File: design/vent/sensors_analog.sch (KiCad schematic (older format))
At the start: 7 parts, among them J1 A-DF 15 A/KG-T2S, U11 SPU01M-15

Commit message: Vent & Injector Board Layout
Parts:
- C18: footprint Diode_SMD:D_0805_2012Metric_Pad0.97x1.50mm_HandSolder -> Capacitors_SMD:C_0805_HandSoldering
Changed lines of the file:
@@
 	4750 2700 4500 2700
 $Comp
-L +5V #PWR085
+L +5V #PWR083
 U 1 1 5AE8176B
 P 4500 2100
-F 0 "#PWR085" H 4500 1950 50  0001 C CNN
+F 0 "#PWR083" H 4500 1950 50  0001 C CNN
 F 1 "+5V" H 4500 2240 50  0000 C CNN
 F 2 "" H 4500 2100 50  0001 C CNN
@@
 $EndComp
 $Comp
-L +11.1V #PWR086
+L +11.1V #PWR084
 U 1 1 5AE81C44
 P 1850 2350
-F 0 "#PWR086" H 1850 2200 50  0001 C CNN
+F 0 "#PWR084" H 1850 2200 50  0001 C CNN
 F 1 "+11.1V" H 1850 2490 50  0000 C CNN
 F 2 "" H 1850 2350 50  0001 C CNN
@@
 	1850 2500 2150 2500
 $Comp
-L GND #PWR087
+L GND #PWR085
 U 1 1 5AE81C4C
 P 2150 2850
-F 0 "#PWR087" H 2150 2600 50  0001 C CNN
+F 0 "#PWR085" H 2150 2600 50  0001 C CNN
 F 1 "GND" H 2150 2700 50  0000 C CNN
 F 2 "" H 2150 2850 50  0001 C CNN
@@
 	2150 2850 2150 2700
 $Comp
-L GND #PWR088
+L GND #PWR086
 U 1 1 5AE81C53
 P 3200 2850
-F 0 "#PWR088" H 3200 2600 50  0001 C CNN
+F 0 "#PWR086" H 3200 2600 50  0001 C CNN
 F 1 "GND" H 3200 2700 50  0000 C CNN
 F 2 "" H 3200 2850 50  0001 C CNN
@@
 	3200 2850 3200 2700
 $Comp
-L +15V #PWR089
+L +15V #PWR087
 U 1 1 5AE81C5A
 P 3600 2300
-F 0 "#PWR089" H 3600 2150 50  0001 C CNN
+F 0 "#PWR087" H 3600 2150 50  0001 C CNN
 F 1 "+15V" H 3600 2440 50  0000 C CNN
 F 2 "" H 3600 2300 50  0001 C CNN
@@
 	4750 4500 4500 4500
 $Comp
-L +5V #PWR090
+L +5V #PWR088
 U 1 1 5AE82545
 P 4500 3900
-F 0 "#PWR090" H 4500 3750 50  0001 C CNN
+F 0 "#PWR088" H 4500 3750 50  0001 C CNN
 F 1 "+5V" H 4500 4040 50  0000 C CNN
 F 2 "" H 4500 3900 50  0001 C CNN
@@
 	6550 2700 6300 2700
 $Comp
-L +5V #PWR091
+L +5V #PWR089
 U 1 1 5AE825E4
 P 6300 2100
-F 0 "#PWR091" H 6300 1950 50  0001 C CNN
+F 0 "#PWR089" H 6300 1950 50  0001 C CNN
 F 1 "+5V" H 6300 2240 50  0000 C CNN
 F 2 "" H 6300 2100 50  0001 C CNN
@@
 	6550 4500 6300 4500
 $Comp
-L +5V #PWR092
+L +5V #PWR090
 U 1 1 5AE8265D
 P 6300 3900
-F 0 "#PWR092" H 6300 3750 50  0001 C CNN
+F 0 "#PWR090" H 6300 3750 50  0001 C CNN
 F 1 "+5V" H 6300 4040 50  0000 C CNN
 F 2 "" H 6300 3900 50  0001 C CNN
@@
 F 0 "C18" H 3525 2800 50  0000 L CNN
 F 1 "4.7uF" H 3525 2600 50  0000 L CNN
-F 2 "Diode_SMD:D_0805_2012Metric_Pad0.97x1.50mm_HandSolder" H 3538 2550 50  0001 C CNN
+F 2 "Capacitors_SMD:C_0805_HandSoldering" H 3538 2550 50  0001 C CNN
 F 3 "" H 3500 2700 50  0001 C CNN
 	1    3500 2700
@@
 $EndComp
 $Comp
-L GND #PWR093
+L GND #PWR091
 U 1 1 5AE9556F
 P 3500 2850
-F 0 "#PWR093" H 3500 2600 50  0001 C CNN
+F 0 "#PWR091" H 3500 2600 50  0001 C CNN
 F 1 "GND" H 3500 2700 50  0000 C CNN
 F 2 "" H 3500 2850 50  0001 C CNN
@@
 (Control power input,\nmay not be connected)
 $Comp
-L +15V #PWR094
+L +15V #PWR092
 U 1 1 5AF096B4
 P 7900 3100
-F 0 "#PWR094" H 7900 2950 50  0001 C CNN
+F 0 "#PWR092" H 7900 2950 50  0001 C CNN
 F 1 "+15V" H 7900 3240 50  0000 C CNN
 F 2 "" H 7900 3100 50  0001 C CNN
@@
 	8950 4000 9300 4000
 $Comp
-L GND #PWR095
+L GND #PWR093
 U 1 1 5AF0A90A
 P 9150 4350
-F 0 "#PWR095" H 9150 4100 50  0001 C CNN
+F 0 "#PWR093" H 9150 4100 50  0001 C CNN
 F 1 "GND" H 9150 4200 50  0000 C CNN
 F 2 "" H 9150 4350 50  0001 C CNN

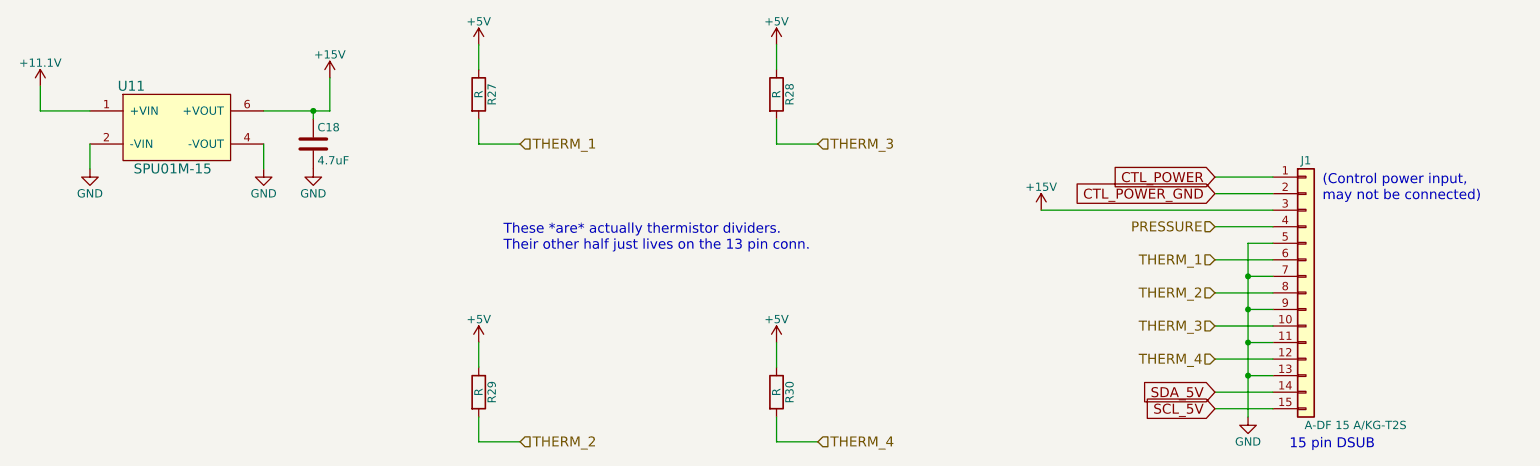
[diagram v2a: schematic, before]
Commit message: Final vent/injector layout + routing
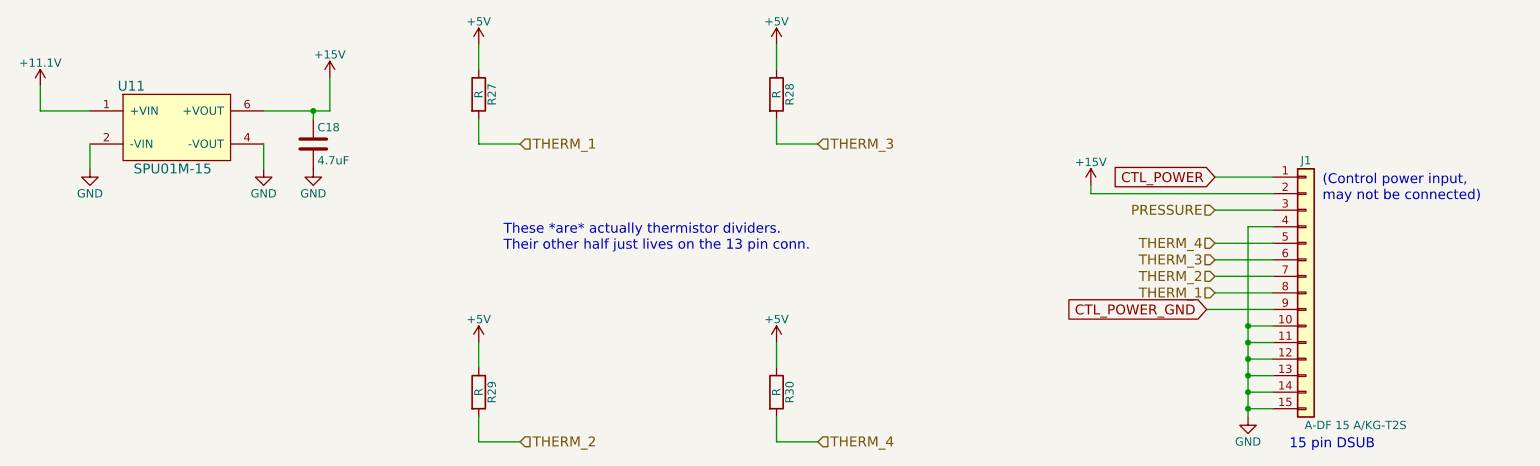
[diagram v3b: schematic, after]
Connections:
- net SCL_5V is gone; now on net GND: J1.15 (Pin_15)
- net SDA_5V is gone; now on net GND: J1.14 (Pin_14)
- net +15V: now also J1.2 (Pin_2); no longer J1.3 (Pin_3)
- net CTL_POWER_GND: now also J1.9 (Pin_9); no longer J1.2 (Pin_2)
- net GND: now also J1.10 (Pin_10), J1.12 (Pin_12), J1.4 (Pin_4); no longer J1.5 (Pin_5), J1.7 (Pin_7), J1.9 (Pin_9)
- net PRESSURE: now also J1.3 (Pin_3); no longer J1.4 (Pin_4)
- net THERM_1: now also J1.8 (Pin_8); no longer J1.6 (Pin_6)
- net THERM_2: now also J1.7 (Pin_7); no longer J1.8 (Pin_8)
- net THERM_3: now also J1.6 (Pin_6); no longer J1.10 (Pin_10)
- net THERM_4: now also J1.5 (Pin_5); no longer J1.12 (Pin_12)
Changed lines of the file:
@@
 $EndComp
 Wire Wire Line
-	3600 2300 3600 2500
-Wire Wire Line
-	3600 2500 3200 2500
+	3600 2500 3600 2300
+Wire Wire Line
+	3200 2500 3600 2500
 $Comp
 L R R29
@@
 Text HLabel 6550 4500 2    60   Input ~ 0
 THERM_4
-Text HLabel 8950 3200 0    60   Input ~ 0
+Text HLabel 8950 3100 0    60   Input ~ 0
 PRESSURE
 $Comp
@@
 Text GLabel 8950 2900 0    60   Input ~ 0
 CTL_POWER
-Text GLabel 8950 3000 0    60   Input ~ 0
+Text GLabel 8900 3700 0    60   Input ~ 0
 CTL_POWER_GND
 Wire Wire Line
 	8950 2900 9300 2900
 Wire Wire Line
-	8950 3000 9300 3000
+	8200 3000 9300 3000
 Text Notes 9600 3050 0    60   ~ 0
 (Control power input,\nmay not be connected)
@@
 L +15V #PWR092
 U 1 1 5AF096B4
-P 7900 3100
-F 0 "#PWR092" H 7900 2950 50  0001 C CNN
-F 1 "+15V" H 7900 3240 50  0000 C CNN
-F 2 "" H 7900 3100 50  0001 C CNN
-F 3 "" H 7900 3100 50  0001 C CNN
-	1    7900 3100
-	1    0    0    -1
-$EndComp
-Wire Wire Line
-	7900 3100 9300 3100
-Wire Wire Line
-	8950 3200 9300 3200
+P 8200 2950
+F 0 "#PWR092" H 8200 2800 50  0001 C CNN
+F 1 "+15V" H 8200 3090 50  0000 C CNN
+F 2 "" H 8200 2950 50  0001 C CNN
+F 3 "" H 8200 2950 50  0001 C CNN
+	1    8200 2950
+	1    0    0    -1
+$EndComp
+Text HLabel 8950 3600 0    60   Input ~ 0
+THERM_1
+Wire Wire Line
+	8950 3400 9300 3400
+Text HLabel 8950 3500 0    60   Input ~ 0
+THERM_2
+Wire Wire Line
+	8950 3600 9300 3600
 Text HLabel 8950 3400 0    60   Input ~ 0
-THERM_1
-Wire Wire Line
-	8950 3400 9300 3400
-Text HLabel 8950 3600 0    60   Input ~ 0
-THERM_2
-Wire Wire Line
-	8950 3600 9300 3600
-Text HLabel 8950 3800 0    60   Input ~ 0
 THERM_3
-Text HLabel 8950 4000 0    60   Input ~ 0
+Text HLabel 8950 3300 0    60   Input ~ 0
 THERM_4
 Wire Wire Line
-	8950 3800 9300 3800
-Wire Wire Line
-	8950 4000 9300 4000
+	9150 3800 9300 3800
+Wire Wire Line
+	9150 4000 9300 4000
 $Comp
 L GND #PWR093
@@
 $EndComp
 Wire Wire Line
-	9150 4350 9150 3300
-Wire Wire Line
-	9150 3300 9300 3300
-Wire Wire Line
-	9300 3500 9150 3500
-Connection ~ 9150 3500
-Wire Wire Line
-	9300 3700 9150 3700
-Connection ~ 9150 3700
+	9150 3200 9150 4350
+Wire Wire Line
+	8950 3300 9300 3300
 Wire Wire Line
 	9300 3900 9150 3900
@@
 	1    0    0    -1
 $EndComp
-Text GLabel 8950 4300 0    60   Input ~ 0
-SCL_5V
-Text GLabel 8950 4200 0    60   Input ~ 0
-SDA_5V
-Wire Wire Line
-	8950 4200 9300 4200
-Wire Wire Line
-	8950 4300 9300 4300
 Text Notes 9400 4550 0    60   ~ 0
 15 pin DSUB
+Wire Wire Line
+	9300 4200 9150 4200
+Connection ~ 9150 4200
+Wire Wire Line
+	9300 4300 9150 4300
+Connection ~ 9150 4300
+Wire Wire Line
+	8200 2950 8200 3000
+Wire Wire Line
+	8950 3100 9300 3100
+Wire Wire Line
+	8950 3500 9300 3500
+Connection ~ 9150 3800
+Connection ~ 9150 4000
+Wire Wire Line
+	8900 3700 9300 3700
+Wire Wire Line
+	9300 3200 9150 3200
 $EndSCHEMATC
